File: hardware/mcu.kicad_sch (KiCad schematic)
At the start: 17 parts, among them J3 USB-C, U1 RP2354A, X1 12MHz

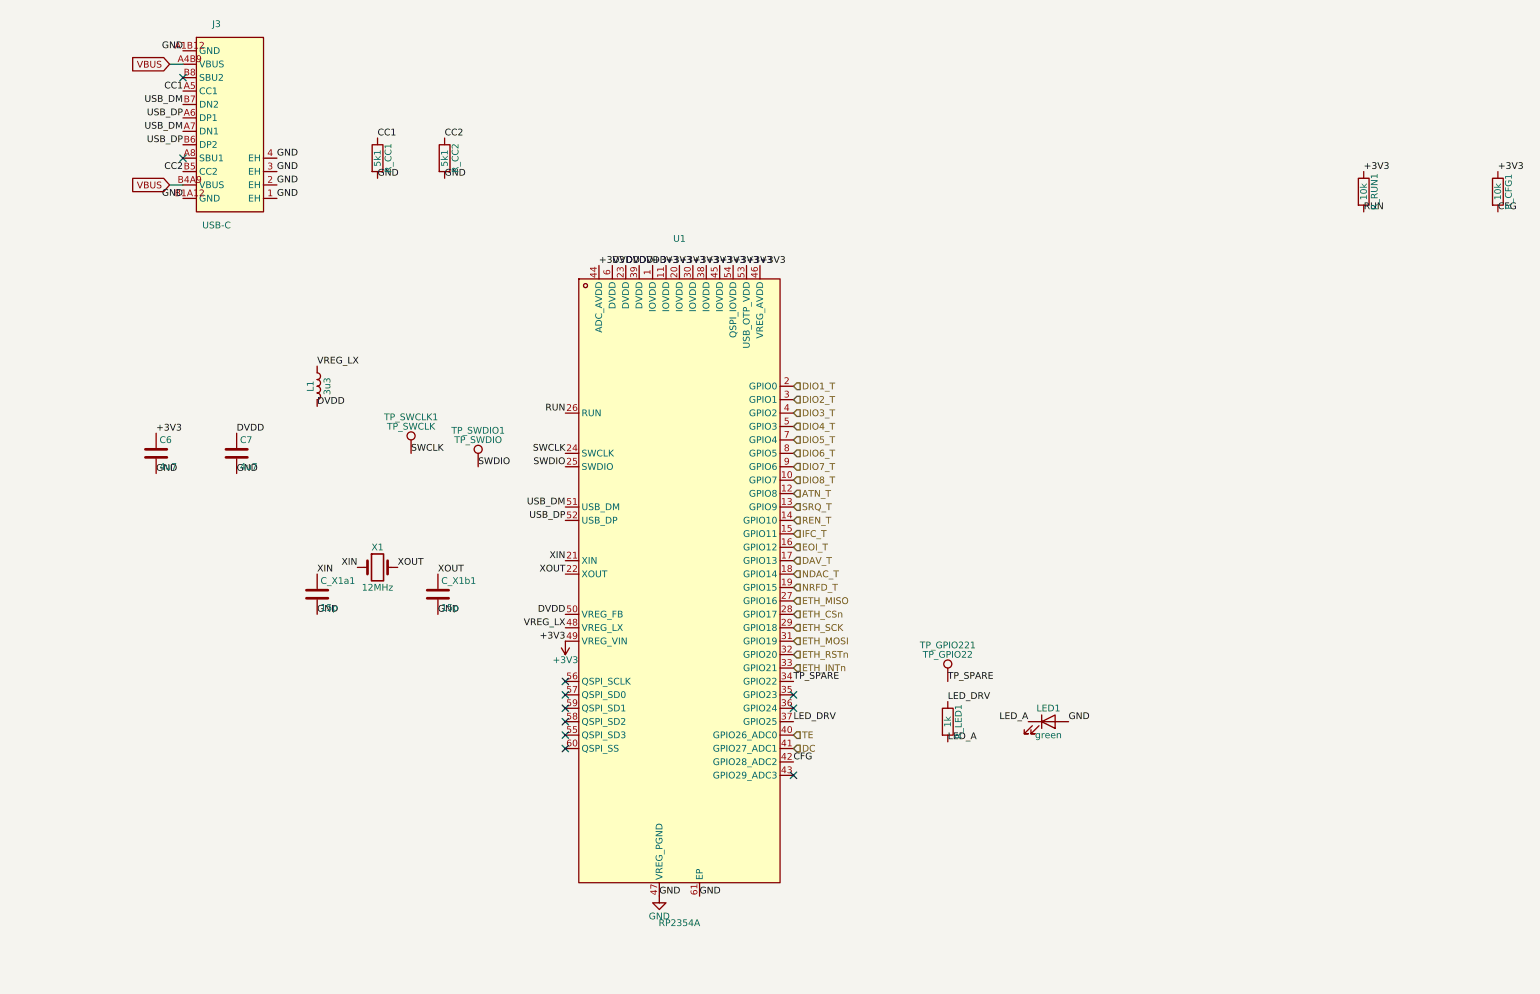
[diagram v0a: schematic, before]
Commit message: hardware: updated board design (reference renumbering, LED polarity fix, crystal symbol upgrade)
Replaces the schematics/PCB/project file with the latest design. Key
changes, verified before committing (netlist-check.py: 124 checks, 0
failures; ERC unchanged at 3 known pin_not_driven findings on W5500 SPI
inputs, same severity-policy artifact as before):

- Component reference designators changed from descriptive names
  (R_ATN, C_3V3, D_BR1, etc.) to plain auto-numbered ones (R15, C9, D1,
  etc.) -- intentional, since descriptive names were ending up on the
  silkscreen; they belong in the BOM instead. docs/netlist-spec.nets
  updated to match via a UUID-verified old-ref -> new-ref mapping (every
  renamed symbol's KiCad UUID was unchanged, confirming these are pure
  renames with no electrical difference), not a hand transcription.
- LED1's wiring was corrected: the old schematic had its anode tied to
  GND and cathode driven by LED_A (backwards -- confirmed via each net's
  pinfunction annotation in the exported netlist, K_1/A_2, which is
  fixed by the Device:LED symbol regardless of reference numbering).
  The new schematic has cathode-to-GND, anode-to-LED_A, the correct
  orientation.
- X1/X2 changed from Device:Crystal (2-pin) to Device:Crystal_GND24
  (4-pin, case-ground on pins 2/4) -- a more accurate symbol for the
  real SMD crystal package. netlist-spec.nets updated accordingly
  (XOUT/ETH_XO now reference pin 3, GND gained the four case pins).

mcu.kicad_sch was supplied separately (missing from the first archive);
confirmed it has no further sub-sheet references and all its symbols'
footprint names resolve against the existing hardware/lib/adapter.pretty/
library, which was deliberately left untouched along with fp-lib-table,
sym-lib-table, and .konnect/ -- none of those changed in this update.
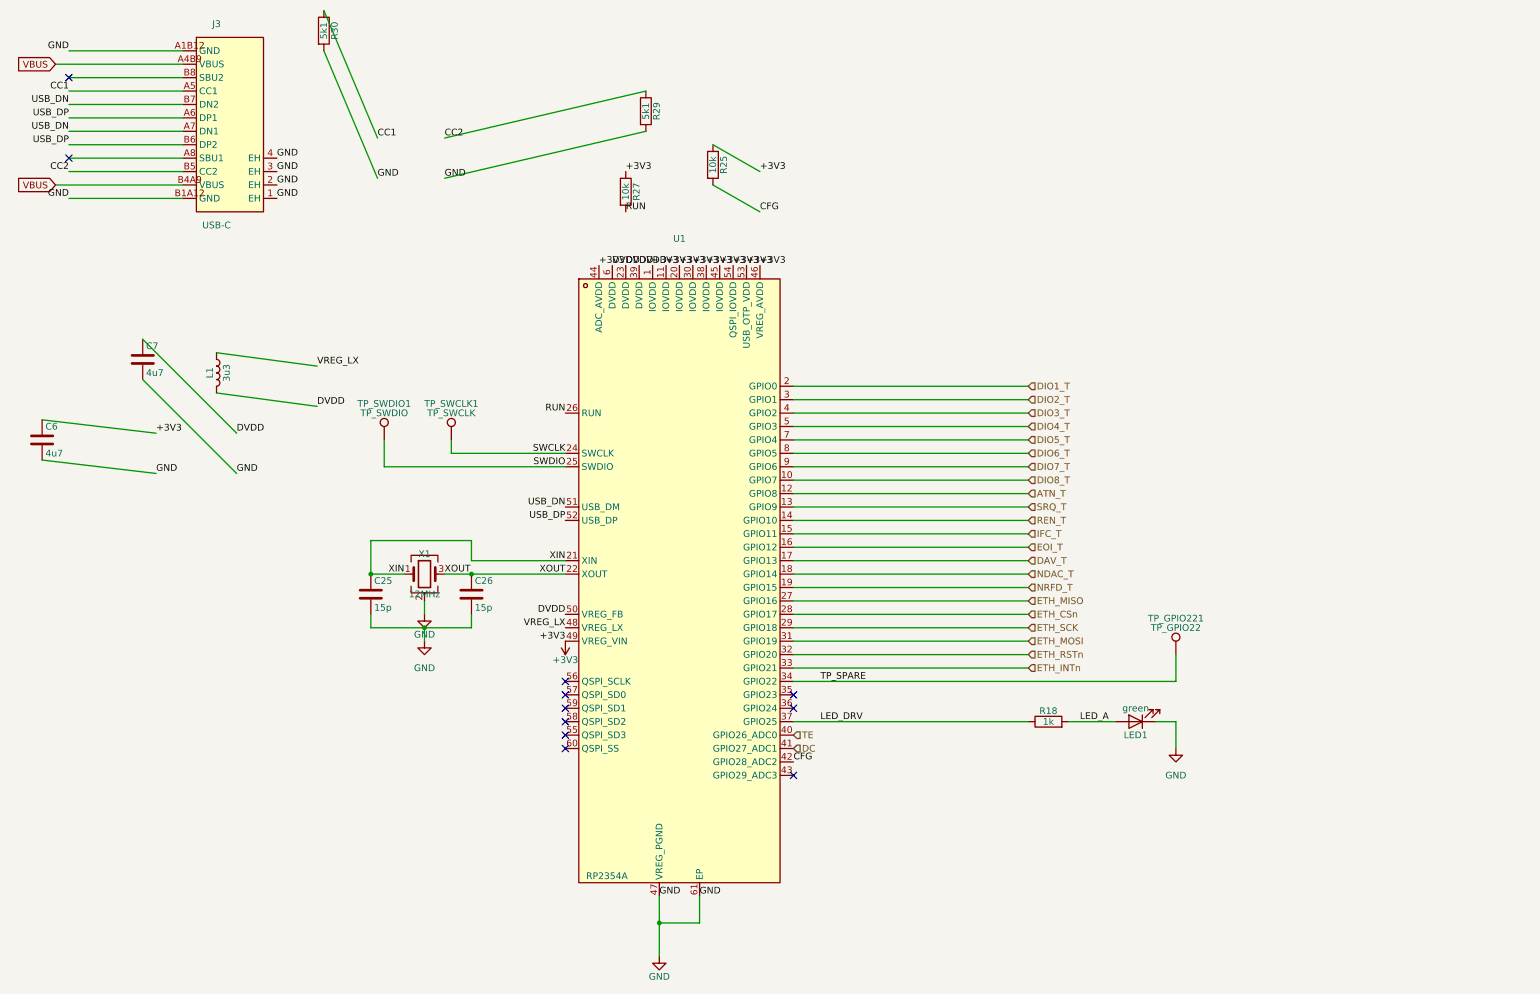
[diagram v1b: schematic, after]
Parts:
- J3: LCSC (none) -> C165948
- U1: LCSC (none) -> C41378174
- X1: symbol Device:Crystal -> Device:Crystal_GND24; LCSC Part (none) -> C7294550; MPN (none) -> CF4012M00012001; Manufacturer (none) -> huaxindianzi
- renumbered C_X1a1 to C25, C_X1b1 to C26, R_LED1 to R18, R_CFG1 to R25, R_RUN1 to R27, R_CC2 to R29, R_CC1 to R30
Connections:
- net GND: now also LED1.1 (K), X1.2 (G), X1.4 (G); no longer LED1.2 (A)
- net LED_A: now also LED1.2 (A); no longer LED1.1 (K)
- net XOUT: now also X1.3; no longer X1.2
- net USB_DM renamed USB_DN
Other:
- moved on the sheet: C25, C26, C6, C7, L1, LED1, R18, R25, R27, R29, R30, TP_GPIO221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
